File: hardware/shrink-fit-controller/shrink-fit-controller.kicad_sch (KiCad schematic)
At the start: 16 parts, among them J1 12V IN (kit wall wart), J2 SSR-100DD input, J3 Bus sense DC+/DC-, J4 Flow switch, J5 E-stop sense, J6 Start button, J7 CAN TTL (Phase 2), J8 MAX31855 (Phase 2), J9 INA228 I2C (Phase 2), Q1 2N3904, U1 ESP32-S3 Super Mini HW-747

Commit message: Schematic rev B: NodeMCU-32S, 24 V primary, lamps off the MCU
Regenerated against docs/pinmap.md. ERC 0 violations, and all 38 U1 pins
verified independently -- nets on the named pins, no-connects on the
rest, flash pins 17/18/19/35/36 explicitly NC.

Changes from rev A: U1 is the NodeMCU-32S (proven symbol and footprint
copied from sln-geo-aux-heat rather than redrawn); MAX31855 header
deleted; power is 24 V in with two LM2596 bucks (5 V logic, 12 V motors
and lamps) rather than a single 12->5; the 220k/10k bus divider and its
filter cap are gone because the INA228 measures bus voltage now; and
lamps, encoder, cycle start/stop, DS18B20 and the TFT are added.

Two bugs ERC caught that reading the code did not.

The pin-geometry regex ran past the end of the NodeMCU symbol into the
CONN symbols appended after it. Those pins are numbered 1-6 and silently
overwrote the MCU's pins 1-6, so GND, TFT_MOSI, SCL and SDA were placed
at the connector's x instead of the MCU's. That is precisely the
wrong-pad failure this project has a standing rule about -- arrived by a
different route, and the 38-pin assert passed anyway because the count
was still 38. The parse is now brace-bounded to the symbol, with an
assert that every pin sits at x = +/-15.24; anything else means it
escaped again.

And all three PWR_FLAGs were landing on GND rather than +5V and +12V,
because I counted connector pin positions by eye instead of computing
them.

Both were found by running ERC rather than by inspection, which is the
argument for generating and checking rather than drawing and trusting.
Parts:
- removed C1: 100nF, symbol shrink-fit-controller:C
- removed R2: 220k, symbol shrink-fit-controller:R
- removed R3: 10k, symbol shrink-fit-controller:R
- added J10: INA228 I2C, symbol shrink-fit-controller:CONN_04
- added J11: DS18B20 1-Wire x2, symbol shrink-fit-controller:CONN_03
- added J12: Round TFT (SPI), symbol shrink-fit-controller:CONN_06
- added J13: PCF8574 + lamp drivers, symbol shrink-fit-controller:CONN_04
- added PS2: LM2596 24V->12V motors, symbol shrink-fit-controller:CONN_04
- J1: value 12V IN (kit wall wart) -> 24V IN (S-250-24)
- J3: value Bus sense DC+/DC- -> Contactor drop relay
- J4: value Flow switch -> Flow sensor (Hall, 0.3-3L); symbol shrink-fit-controller:CONN_02 -> shrink-fit-controller:CONN_03
- J6: value Start button -> CYCLE START
- J7: value CAN TTL (Phase 2) -> CYCLE STOP; symbol shrink-fit-controller:CONN_04 -> shrink-fit-controller:CONN_02
- J8: value MAX31855 (Phase 2) -> Encoder EC11
- J9: value INA228 I2C (Phase 2) -> CAN isolated stack
- PS1: value LM2596 module 12V->5V -> LM2596 24V->5V logic
- U1: value ESP32-S3 Super Mini HW-747 -> NodeMCU-32S (ESP32, 38-pin); symbol shrink-fit-controller:ESP32-S3-SuperMini-HW747 -> shrink-fit-controller:NodeMCU-32S
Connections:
- net BUS_SENSE is gone; now on net SCL: U1.3 (P22)
- net BUS_V+ is gone; now on net +12V: J3.1
- net +12V: now also PS2.3; no longer J1.1, PS1.1
- net +3V3: now also U1.20 (3V3), J10.1, J11.1, J12.1, J13.1; no longer J4.1, J7.1, U1.16 (3V3)
- net +5V: now also J4.1, U1.38 (5V); no longer U1.18 (5V)
- net CAN_RX: now also J9.4, U1.26 (P32); no longer J7.4, U1.7 (GPIO5)
- net CAN_TX: now also J9.3, U1.31 (P14); no longer J7.3, U1.6 (GPIO4)
- net ESTOP_SENSE: now also U1.22 (P36_VP); no longer U1.9 (GPIO7)
- net GND: now also J4.2, U1.1 (GND), U1.33 (GND), U1.37 (GND), U1.7 (GND), J10.2, J11.2, J12.2, J13.2, PS2.2, PS2.4; no longer J3.2, U1.17 (GND)
- net SCL: now also J10.4, J13.4; no longer J9.4, U1.11 (GPIO9)
- net SDA: now also U1.6 (P21), J10.3, J13.3; no longer J9.3, U1.10 (GPIO8)
- net SSR_DRV: now also U1.13 (P4); no longer U1.12 (GPIO10)
- net TFT_MOSI: now reaches U1.2 (P23)
- net TFT_MOSI: now also J12.6
- net FLOW_SW renamed ENC_B
- net ENC_B: now also J8.4; no longer J4.2
- net START_BTN: no longer names the net of U1.4 (TX0)
- net START_BTN: no longer J6.1
- removed net TC_CS: J8.4, U1.13 (GPIO11)
- net TC_MISO: no longer names the net of U1.15 (P2)
- net TC_MISO: no longer J8.5
- net TC_SCK: no longer names the net of U1.14 (P0)
- net TC_SCK: no longer J8.3
- new net +24V: J1.1, PS1.1, PS2.1
- new net CYCLE_START: J6.1, U1.24 (P34)
- new net CYCLE_STOP: J7.1, U1.25 (P35)
- new net ENC_A: J8.3, U1.34 (P13)
- new net ENC_SW: J8.5, U1.16 (P15)
- new net FLOW_PULSE: J4.3, U1.23 (P39_VN)
- new net OW_DATA: J11.3, U1.27 (P33)
- new net RELAY_K: J3.2, U1.12 (P16)
- new net TFT_CS: J12.3, U1.10 (P5)
- new net TFT_DC: J12.4, U1.11 (P17)
- new net TFT_SCK: J12.5, U1.9 (P18)
- no-connect marks 3 -> 14
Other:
- note added: "34/35/36/39 (pins 24,25,22,23) are INPUT ONLY with NO internal pull-up. Every button and sensor on them needs an external 10k to 3V3 or it floats and reads randomly."
- note added: "Bus voltage now comes from the INA228 (J10), not a discrete divider. The old 220k/10k and its filter cap are deleted."
- note added: "FLASH PINS - NPTH, NO COPPER: pins 17,18,19,35,36 (SD1,SD0,CLK,SD2,SD3) are the internal SPI flash bus, GPIO6-11. Holes with no pad. Do NOT delete the holes or the module cannot seat."
- note added: "GND IS DC-. The controller floats with the bus. No USB while energised; no earthed scope ground clip - differential probe or a non-contact pickup loop only."
- note added: "LAMPS ARE NOT ON THE MCU. Three 12V panel lamps hang off a PCF8574 (J13) via 2N7002 MOSFETs. The expander sources only ~100uA when high, which is too little for a 2N3904 base - a MOSFET gate is voltage-driven and does not care."
- note added: "MAINS START IS NOT HERE. It is hardwired in the contactor coil circuit (requirements 6.9) and must never reach the MCU: firmware must not be able to energise mains by itself."
- note added: "SPARE: P25 (28), P26 (29), P27 (30) - freed by moving lamps to the expander. P0/P2/P12 are strapping pins, usable only with care."
- note added: "SSR-100DD input 3-32V from +12V, Q1 low-side. P4 delivers the voltage STEP (CR-05); the AC contactor never does - a Royer fed a slow ramp shoots through and kills the IRFP260Ns."
- note added: "WIRE BY PIN NAME, NEVER BY NUMBER. On this symbol pin NUMBER 26 is the pin NAMED P32 - numbers are header positions. Verify every net against the pad number in docs/pinmap.md after layout; ERC will not catch it."
- note removed: "Divider 220k/10k = 23:1 (180k not stocked). Calibrate with testrig 'cal <V>'. C1 is not optional: sensing beside a kW oscillator (R-11)."
- note removed: "GND IS DC-. The controller floats with the bus (SR-11 bond withdrawn). No USB while energised; no earthed scope ground clip - differential probe only."
- note removed: "GPIO3 reserved: Stage-4 encoder."
- note removed: "J4 flow: switch to 3V3, firmware INPUT_PULLDOWN, active high = flow proven. J5/J6: contacts to GND, INPUT_PULLUP, active low."
- note removed: "Phase 2 headers J7/J8/J9: footprints reserved, unpopulated. CAN stack (ADUM1201 + B0505S + SN65HVD230) is off-board - isolation required. INA228 shunt value is a PLACEHOLDER until VR-11 four-wire cal."
- note removed: "SSR-100DD input 3-32V, fed from +12V; Q1 low-side. GPIO10 delivers the voltage STEP (CR-05) - CAN sets bus volts, never enables output."
- note removed: "WIRE BY PIN NAME, NEVER BY NUMBER. U1 numbers are header positions: GPIO1 = pin 3, GPIO10 (SSR drive) = pin 12. Verify pads in the .kicad_pcb after layout."
- moved on the sheet: J1, J2, J3, J5, J6, J8, J9, PS1, Q1, R1

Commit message: Footprints assigned; netlist verified against pad numbers
18 components, 0 without a footprint, ERC 0 violations, and all 20
critical nets confirmed landing on the correct U1 PIN NUMBER in the
exported netlist -- CAN_RX on 26, SSR_DRV on 13, ENC_A on 34. That is
the check that catches the wrong-pad failure; ERC does not.

Generated project-local 2.54 mm headers rather than using KiCad's stock
PinHeader library. The stock parts use 1.7 mm pads on a 1.0 mm drill,
which on this shop's bit set snaps UP to 1.181 mm and leaves a 0.259 mm
annulus against pcbmill's 0.25 mm gate -- passing by 9.5 microns, which
is not a margin, it is luck. 1.78 mm pads give 0.299 mm and match the
NodeMCU-32S_38pin_THT footprint already proven in this project. Same
drill, same pitch, 80 microns more copper.

Worth noting this board never carries the 67 A bus -- that path is
entirely off-board -- so 2.54 mm headers are adequate throughout and no
terminal blocks are needed.
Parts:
- J1, J2, J3, J5, J6, J7: footprint (none) -> shrink-fit-controller:PinHeader_1x02_P2.54mm_Vertical_1.78pad
- J10, J13, J9, PS1, PS2: footprint (none) -> shrink-fit-controller:PinHeader_1x04_P2.54mm_Vertical_1.78pad
- J11, J4: footprint (none) -> shrink-fit-controller:PinHeader_1x03_P2.54mm_Vertical_1.78pad
- J12: footprint (none) -> shrink-fit-controller:PinHeader_1x06_P2.54mm_Vertical_1.78pad
- J8: footprint (none) -> shrink-fit-controller:PinHeader_1x05_P2.54mm_Vertical_1.78pad
- Q1: footprint (none) -> Package_TO_SOT_THT:TO-92_Inline
- R1: footprint (none) -> Resistor_THT:R_Axial_DIN0207_L6.3mm_D2.5mm_P10.16mm_Horizontal
- U1: footprint (none) -> shrink-fit-controller:NodeMCU-32S_38pin_THT
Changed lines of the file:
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@@
 			)
 		)
-		(property "Footprint" ""
+		(property "Footprint" "shrink-fit-controller:PinHeader_1x02_P2.54mm_Vertical_1.78pad"
 			(at 35.56 25.4 0)
 			(hide yes)			(show_name no)
@@
 			)
 		)
-		(property "Footprint" ""
+		(property "Footprint" "shrink-fit-controller:PinHeader_1x04_P2.54mm_Vertical_1.78pad"
 			(at 35.56 38.1 0)
 			(hide yes)			(show_name no)
@@
 			)
 		)
-		(property "Footprint" ""
+		(property "Footprint" "shrink-fit-controller:PinHeader_1x04_P2.54mm_Vertical_1.78pad"
 			(at 35.56 55.88 0)
 			(hide yes)			(show_name no)
@@
 			)
 		)
-		(property "Footprint" ""
+		(property "Footprint" "shrink-fit-controller:PinHeader_1x02_P2.54mm_Vertical_1.78pad"
 			(at 35.56 73.66 0)
 			(hide yes)			(show_name no)
@@
 			)
 		)
-		(property "Footprint" ""
+		(property "Footprint" "shrink-fit-controller:PinHeader_1x02_P2.54mm_Vertical_1.78pad"
 			(at 35.56 83.82 0)
 			(hide yes)			(show_name no)
@@
 			)
 		)
-		(property "Footprint" ""
+		(property "Footprint" "shrink-fit-controller:PinHeader_1x03_P2.54mm_Vertical_1.78pad"
 			(at 35.56 93.98 0)
 			(hide yes)			(show_name no)
@@
 			)
 		)
-		(property "Footprint" ""
+		(property "Footprint" "shrink-fit-controller:PinHeader_1x02_P2.54mm_Vertical_1.78pad"
 			(at 35.56 106.68 0)
 			(hide yes)			(show_name no)
@@
 			)
 		)
-		(property "Footprint" ""
+		(property "Footprint" "shrink-fit-controller:PinHeader_1x02_P2.54mm_Vertical_1.78pad"
 			(at 35.56 116.84 0)
 			(hide yes)			(show_name no)
@@
 			)
 		)
-		(property "Footprint" ""
+		(property "Footprint" "shrink-fit-controller:PinHeader_1x02_P2.54mm_Vertical_1.78pad"
 			(at 35.56 127.0 0)
 			(hide yes)			(show_name no)
@@
 			)
 		)
-		(property "Footprint" ""
+		(property "Footprint" "shrink-fit-controller:PinHeader_1x05_P2.54mm_Vertical_1.78pad"
 			(at 35.56 137.16 0)
 			(hide yes)			(show_name no)
@@
 			)
 		)
-		(property "Footprint" ""
+		(property "Footprint" "shrink-fit-controller:PinHeader_1x04_P2.54mm_Vertical_1.78pad"
 			(at 35.56 154.94 0)
 			(hide yes)			(show_name no)
@@
 			)
 		)
-		(property "Footprint" ""
+		(property "Footprint" "shrink-fit-controller:PinHeader_1x04_P2.54mm_Vertical_1.78pad"
 			(at 35.56 172.72 0)
 			(hide yes)			(show_name no)
@@
 			)
 		)
-		(property "Footprint" ""
+		(property "Footprint" "shrink-fit-controller:PinHeader_1x03_P2.54mm_Vertical_1.78pad"
 			(at 35.56 190.5 0)
 			(hide yes)			(show_name no)
@@
 			)
 		)
-		(property "Footprint" ""
+		(property "Footprint" "shrink-fit-controller:PinHeader_1x06_P2.54mm_Vertical_1.78pad"
 			(at 35.56 203.2 0)
 			(hide yes)			(show_name no)
@@
 			)
 		)
-		(property "Footprint" ""
+		(property "Footprint" "shrink-fit-controller:PinHeader_1x04_P2.54mm_Vertical_1.78pad"
 			(at 35.56 226.06 0)
 			(hide yes)			(show_name no)
@@
 			)
 		)
-		(property "Footprint" ""
+		(property "Footprint" "shrink-fit-controller:NodeMCU-32S_38pin_THT"
 			(at 127.0 127.0 0)
 			(hide yes)			(show_name no)
@@
 			)
 		)
-		(property "Footprint" ""
+		(property "Footprint" "Resistor_THT:R_Axial_DIN0207_L6.3mm_D2.5mm_P10.16mm_Horizontal"
 			(at 200.66 81.28 0)
 			(hide yes)			(show_name no)
@@
 			)
 		)
-		(property "Footprint" ""
+		(property "Footprint" "Package_TO_SOT_THT:TO-92_Inline"
 			(at 213.36 81.28 0)
 			(hide yes)			(show_name no)

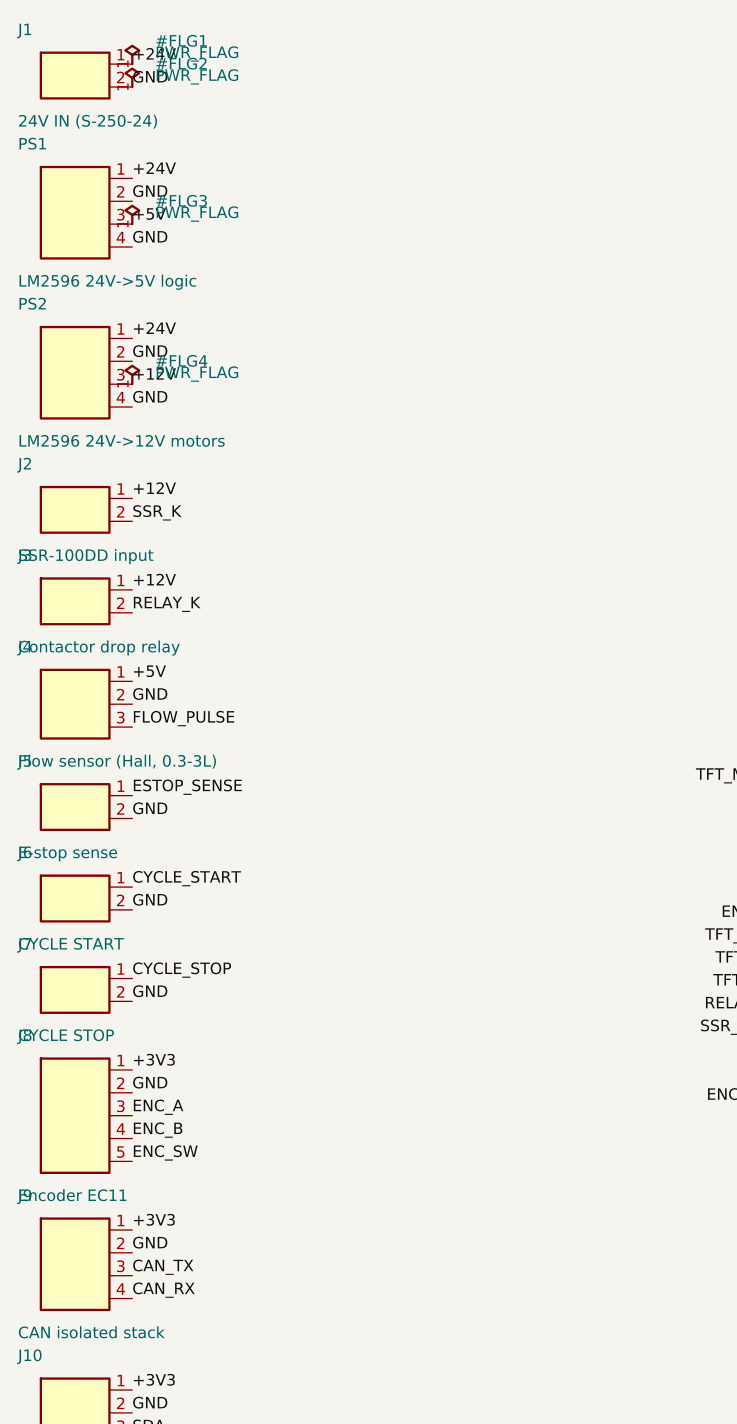
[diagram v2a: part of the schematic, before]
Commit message: Real footprints for the LM2596 modules and the EC11 -- both were placeholders
Scott caught both. I had used generic 1x04 and 1x05 headers, which
silently encoded a decision I never raised: that the buck modules and
the encoder mount OFF the board and the headers are just wiring to them.

LM2596: the proven LM2596_Module_THT footprint already existed in
sln-geo-aux-heat, same source as the NodeMCU footprint -- 2.0 mm pads on
a 1.0 mm drill, 0.410 mm annulus. Modules now mount on the board, which
deletes eight flying leads. Pin order IN+/IN-/OUT+/OUT- confirmed from
the source symbol before wiring, because a swapped in/out on a buck
destroys it.

EC11: a 1x05 header could not map onto the real part at all. The KiCad
footprint's pads are named A/B/C/S1/S2/MP -- letters, not digits -- so a
numbered header symbol has nothing to attach to. Added a proper
RotaryEncoder_EC11 symbol with matching pin numbers and wired it the way
the part works: C is the common and goes to GND, A and B are the
quadrature contacts, S1/S2 are the push switch. There is no +3V3 pin on
an encoder; the pull-ups are the MCU's internal ones, and GPIO 13/19/15
all support them where 34-39 would not have.

Also fixed a modelling error in the LM2596 symbol: OUT- was declared a
power OUTPUT. It is the return, tied to IN- inside the module. With one
buck that is harmless; with two it makes GND a net with three drivers,
which is how ERC found it.

ERC 0 violations, 18 components all with footprints, EC11 netlist
verified pad by pad.
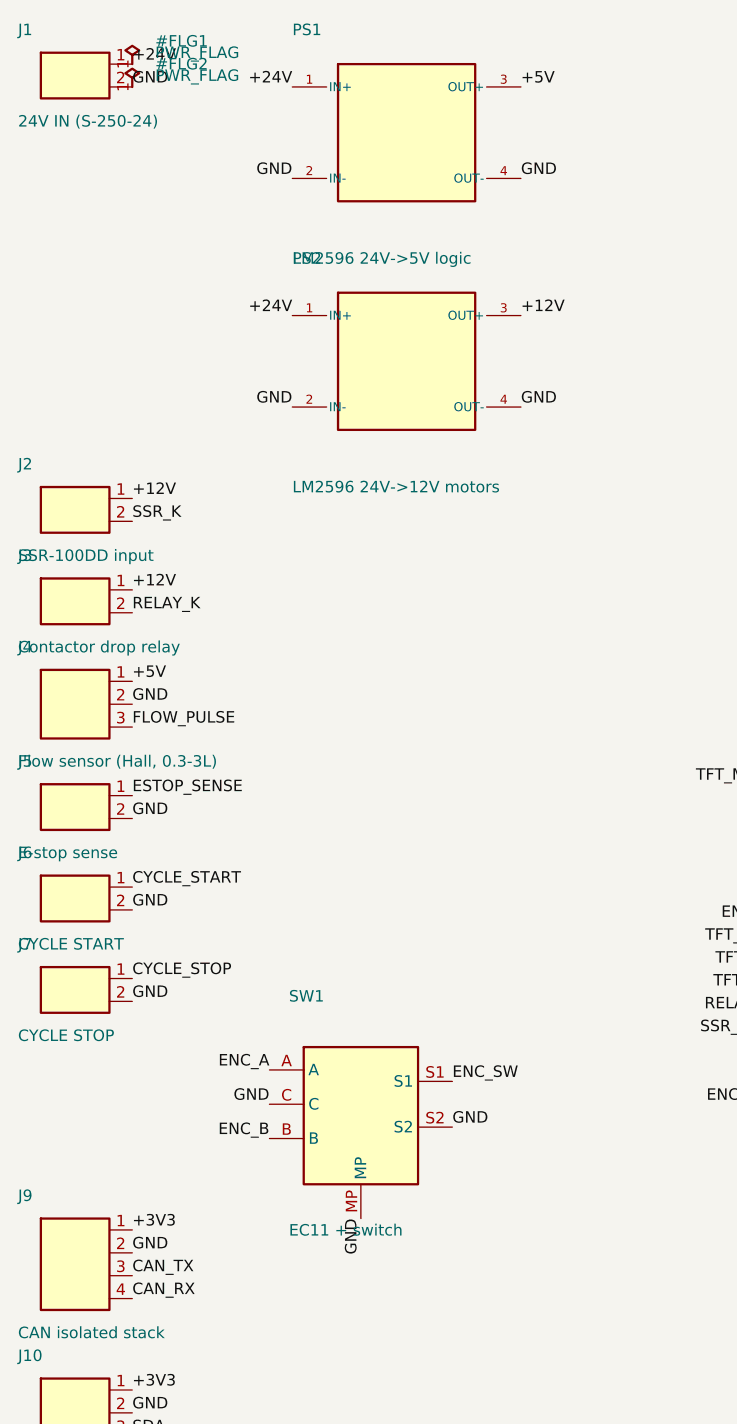
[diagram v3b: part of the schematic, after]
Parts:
- removed J8: Encoder EC11, shrink-fit-controller:PinHeader_1x05_P2.54mm_Vertical_1.78pad, symbol shrink-fit-controller:CONN_05
- added SW1: EC11 + switch, Rotary_Encoder:RotaryEncoder_Alps_EC11E-Switch_Vertical_H20mm, symbol shrink-fit-controller:RotaryEncoder_EC11
- PS1: value LM2596 24V->5V logic -> LM2596 24V->5V logic; footprint shrink-fit-controller:PinHeader_1x04_P2.54mm_Vertical_1.78pad -> shrink-fit-controller:LM2596_Module_THT; symbol shrink-fit-controller:CONN_04 -> shrink-fit-controller:LM2596_Module
- PS2: value LM2596 24V->12V motors -> LM2596 24V->12V motors; footprint shrink-fit-controller:PinHeader_1x04_P2.54mm_Vertical_1.78pad -> shrink-fit-controller:LM2596_Module_THT; symbol shrink-fit-controller:CONN_04 -> shrink-fit-controller:LM2596_Module
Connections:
- net ENC_A: now also SW1.A
- net ENC_B: now also SW1.B
- net ENC_SW: now also SW1.S1
- net GND: now also SW1.C, SW1.MP, SW1.S2

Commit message: PCF8574 and 2N7002 lamp drivers on the board as real parts
The expander was a 4-pin header standing in for a decision. It is now a
DIP-16 with real pin numbers so the stock Package_DIP footprint maps
1:1, A0-A2 grounded for 0x20 (INA228 is at 0x40, no collision), 100 nF
decoupling, and three 2N7002 low-side drivers. J13 becomes the lamp
connector: +12V plus one cathode per lamp.

The PCF8574 has no firmware; lamp logic lives in the ESP32, which
writes one byte to 0x20. Recorded on the sheet that firmware should
rewrite that byte every loop rather than only on change -- the expander
holds its outputs if the MCU hangs, and a refreshed byte turns a hang
into a lamp that stops responding instead of one that lies.

Also noted the boot behaviour rather than fighting it: the PCF8574
powers up with all outputs HIGH, so all three lamps light for the ~100
ms before the first write. That is a free bulb test.

2N7002 is SOT-23, the first SMD part on an otherwise THT board. On a
single-sided milled board it goes on B.Cu flipped; noted on the sheet.
Chosen over a TO-92 because there are 50 in stock at RB-12 and the
gate-drive argument for a MOSFET here is not negotiable.

ERC 0 violations, 23 components all with footprints, every new net
verified pad by pad in the exported netlist.
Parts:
- added C2: 100nF, Capacitor_THT:C_Disc_D5.0mm_W2.5mm_P5.00mm, symbol shrink-fit-controller:C
- added Q2, Q3, Q4: 2N7002, Package_TO_SOT_SMD:SOT-23, symbol shrink-fit-controller:Q_2N7002
- added U2: PCF8574 (0x20), Package_DIP:DIP-16_W7.62mm, symbol shrink-fit-controller:PCF8574
- J13: value PCF8574 + lamp drivers -> LAMPS 12V G / A / R
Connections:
- net +12V: now also J13.1
- net +3V3: now also C2.1, U2.16 (VDD); no longer J13.1
- net GND: now also C2.2, Q2.2 (S), Q3.2 (S), Q4.2 (S), U2.1 (A0), U2.2 (A1), U2.3 (A2), U2.8 (VSS); no longer J13.2
- net SCL: now also U2.14 (SCL); no longer J13.4
- net SDA: now also U2.15 (SDA); no longer J13.3
- new net LAMP_A: J13.3, Q3.3 (D)
- new net LAMP_A_DRV: Q3.1 (G), U2.5 (P1)
- new net LAMP_G: J13.2, Q2.3 (D)
- new net LAMP_G_DRV: Q2.1 (G), U2.4 (P0)
- new net LAMP_R: J13.4, Q4.3 (D)
- new net LAMP_R_DRV: Q4.1 (G), U2.6 (P2)
- no-connect marks 14 -> 20
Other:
- note added: "Lamps: anode to +12V (J13.1), cathode to the 2N7002 drain. Output LOW at the expander = lamp OFF; HIGH = ON. 2N7002 is SOT-23 SMD - on a single-sided milled board it goes on B.Cu, flipped."
